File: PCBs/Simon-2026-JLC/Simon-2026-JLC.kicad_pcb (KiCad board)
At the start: 2 copper layers, 65 x 65 mm, 23 parts, among them IC2 MSPM0G3507SPTR, J1 Conn_01x09, J2 Conn_01x05, SW1 SW_SPST, SW2 SW_SPST, SW3 SW_SPST, SW4 SW_SPST, SW5 SW_SPDT, U1 LIS2HH12

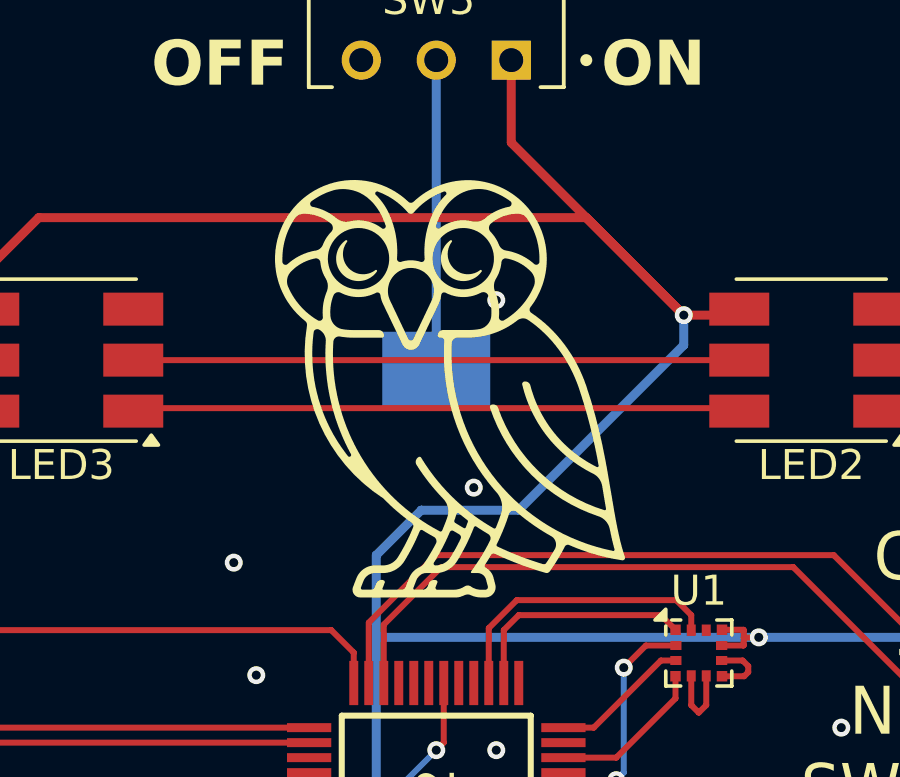
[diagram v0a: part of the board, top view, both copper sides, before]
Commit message: 2026 updated name for Simon PCB
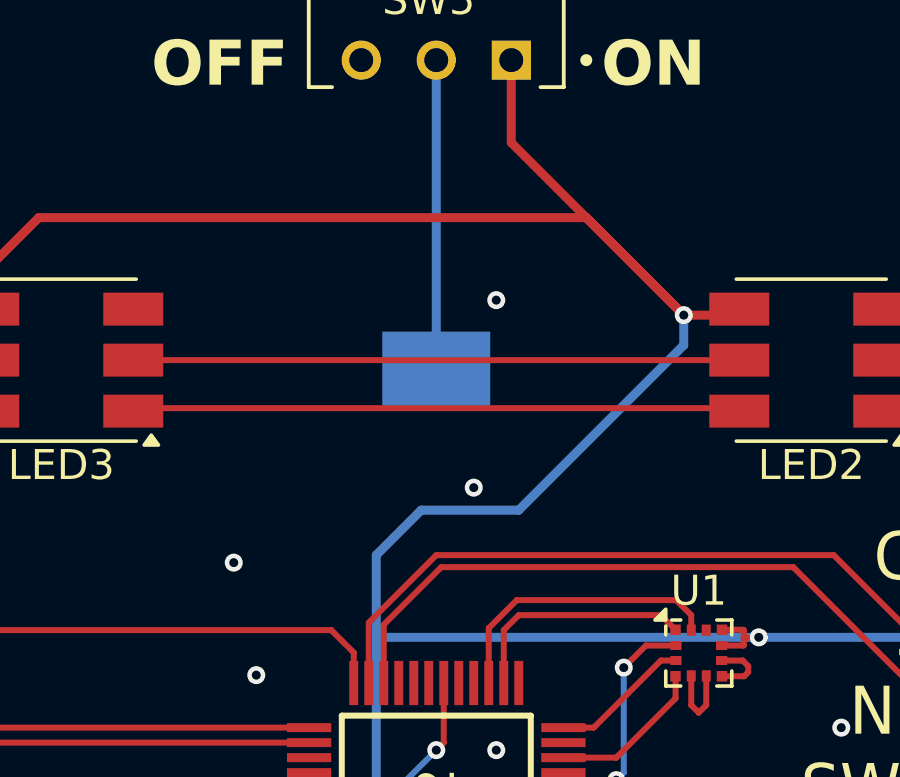
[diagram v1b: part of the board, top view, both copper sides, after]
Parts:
- removed REF**: RICE_OWL_LOGO, ELEC327-Kicad:RICE_OWL_LOGO
